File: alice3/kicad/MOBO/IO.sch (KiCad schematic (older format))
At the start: 12 parts, among them CON1 SD_Card, SW2 SOFT RESET, SW3 POWER, U6 MiniM4-D40, U7 DFROBOT_FTDI_BASIC

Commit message: Remove on/off switch.
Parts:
- removed SW3: POWER, Buttons_Switches_ThroughHole:SW_SPDT, symbol SPST
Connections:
- wire segments 76 -> 74
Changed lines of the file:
@@
 $EndDescr
 $Comp
-L +3.3V #PWR017
+L +3.3V #PWR019
 U 1 1 5689970E
 P 900 2900
-F 0 "#PWR017" H 900 2750 50  0001 C CNN
+F 0 "#PWR019" H 900 2750 50  0001 C CNN
 F 1 "+3.3V" H 900 3040 50  0000 C CNN
 F 2 "" H 900 2900 60  0000 C CNN
@@
 $EndComp
 $Comp
-L GND #PWR018
+L GND #PWR020
 U 1 1 5689975D
 P 2400 4600
-F 0 "#PWR018" H 2400 4350 50  0001 C CNN
+F 0 "#PWR020" H 2400 4350 50  0001 C CNN
 F 1 "GND" H 2400 4450 50  0000 C CNN
 F 2 "" H 2400 4600 60  0000 C CNN
@@
 NoConn ~ 7450 4700
 $Comp
-L GND #PWR019
+L GND #PWR021
 U 1 1 56899C9B
 P 8350 5900
-F 0 "#PWR019" H 8350 5650 50  0001 C CNN
+F 0 "#PWR021" H 8350 5650 50  0001 C CNN
 F 1 "GND" H 8350 5750 50  0000 C CNN
 F 2 "" H 8350 5900 60  0000 C CNN
@@
 $EndComp
 $Comp
-L +3.3V #PWR020
+L +3.3V #PWR022
 U 1 1 56899CD4
 P 8450 4050
-F 0 "#PWR020" H 8450 3900 50  0001 C CNN
+F 0 "#PWR022" H 8450 3900 50  0001 C CNN
 F 1 "+3.3V" H 8450 4190 50  0000 C CNN
 F 2 "" H 8450 4050 60  0000 C CNN
@@
 $EndComp
 $Comp
-L GND #PWR021
+L GND #PWR023
 U 1 1 568A1142
 P 900 4200
-F 0 "#PWR021" H 900 3950 50  0001 C CNN
+F 0 "#PWR023" H 900 3950 50  0001 C CNN
 F 1 "GND" H 900 4050 50  0000 C CNN
 F 2 "" H 900 4200 60  0000 C CNN
@@
 $EndComp
 $Comp
-L GND #PWR022
+L GND #PWR024
 U 1 1 568A2172
 P 5650 2550
-F 0 "#PWR022" H 5650 2300 50  0001 C CNN
+F 0 "#PWR024" H 5650 2300 50  0001 C CNN
 F 1 "GND" H 5650 2400 50  0000 C CNN
 F 2 "" H 5650 2550 60  0000 C CNN
@@
 $EndComp
 $Comp
-L GND #PWR023
+L GND #PWR025
 U 1 1 568A21B9
 P 6650 3150
-F 0 "#PWR023" H 6650 2900 50  0001 C CNN
+F 0 "#PWR025" H 6650 2900 50  0001 C CNN
 F 1 "GND" H 6650 3000 50  0000 C CNN
 F 2 "" H 6650 3150 60  0000 C CNN
@@
 $EndComp
 $Comp
-L +5V #PWR024
+L +5V #PWR026
 U 1 1 568DC45F
-P 8100 2700
-F 0 "#PWR024" H 8100 2550 50  0001 C CNN
-F 1 "+5V" H 8100 2840 50  0000 C CNN
-F 2 "" H 8100 2700 60  0000 C CNN
-F 3 "" H 8100 2700 60  0000 C CNN
-	1    8100 2700
+P 7000 2850
+F 0 "#PWR026" H 7000 2700 50  0001 C CNN
+F 1 "+5V" H 7000 2990 50  0000 C CNN
+F 2 "" H 7000 2850 60  0000 C CNN
+F 3 "" H 7000 2850 60  0000 C CNN
+	1    7000 2850
 	1    0    0    -1
 $EndComp
@@
 	5500 3150 5650 3150
 Wire Wire Line
-	8100 2850 8100 2700
-Wire Wire Line
 	2400 1600 2400 2000
 Wire Wire Line
@@
 Text GLabel 4000 2200 2    60   Input ~ 0
 /BUSACK
-$Comp
-L SPST SW3
-U 1 1 56A02251
-P 7500 2850
-F 0 "SW3" H 7500 2950 50  0000 C CNN
-F 1 "POWER" H 7500 2750 50  0000 C CNN
-F 2 "Buttons_Switches_ThroughHole:SW_SPDT" H 7500 2850 50  0001 C CNN
-F 3 "" H 7500 2850 50  0000 C CNN
-	1    7500 2850
-	1    0    0    -1
-$EndComp
-Wire Wire Line
-	8000 2850 8100 2850
 Wire Wire Line
 	7000 2850 6650 2850
@@
 	2450 4000 2700 4000
 $Comp
-L +3.3V #PWR025
+L +3.3V #PWR027
 U 1 1 56A03E02
 P 2400 1600
-F 0 "#PWR025" H 2400 1450 50  0001 C CNN
+F 0 "#PWR027" H 2400 1450 50  0001 C CNN
 F 1 "+3.3V" H 2400 1740 50  0000 C CNN
 F 2 "" H 2400 1600 60  0000 C CNN
@@
 $EndComp
 $Comp
-L GND #PWR026
+L GND #PWR028
 U 1 1 56A03E72
 P 1750 2200
-F 0 "#PWR026" H 1750 1950 50  0001 C CNN
+F 0 "#PWR028" H 1750 1950 50  0001 C CNN
 F 1 "GND" H 1750 2050 50  0000 C CNN
 F 2 "" H 1750 2200 60  0000 C CNN

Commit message: Before removing DFROBOT.
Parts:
- removed C3: 0.1µ, Capacitors_ThroughHole:C_Disc_D6_P5, symbol C
- renumbered C4 to C3
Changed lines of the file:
@@
 $EndDescr
 $Comp
-L +3.3V #PWR019
+L +3.3V #PWR19
 U 1 1 5689970E
 P 900 2900
-F 0 "#PWR019" H 900 2750 50  0001 C CNN
+F 0 "#PWR19" H 900 2750 50  0001 C CNN
 F 1 "+3.3V" H 900 3040 50  0000 C CNN
 F 2 "" H 900 2900 60  0000 C CNN
@@
 $EndComp
 $Comp
-L GND #PWR020
+L GND #PWR22
 U 1 1 5689975D
 P 2400 4600
-F 0 "#PWR020" H 2400 4350 50  0001 C CNN
+F 0 "#PWR22" H 2400 4350 50  0001 C CNN
 F 1 "GND" H 2400 4450 50  0000 C CNN
 F 2 "" H 2400 4600 60  0000 C CNN
@@
 NoConn ~ 7450 4700
 $Comp
-L GND #PWR021
+L GND #PWR26
 U 1 1 56899C9B
 P 8350 5900
-F 0 "#PWR021" H 8350 5650 50  0001 C CNN
+F 0 "#PWR26" H 8350 5650 50  0001 C CNN
 F 1 "GND" H 8350 5750 50  0000 C CNN
 F 2 "" H 8350 5900 60  0000 C CNN
@@
 $EndComp
 $Comp
-L +3.3V #PWR022
+L +3.3V #PWR27
 U 1 1 56899CD4
 P 8450 4050
-F 0 "#PWR022" H 8450 3900 50  0001 C CNN
+F 0 "#PWR27" H 8450 3900 50  0001 C CNN
 F 1 "+3.3V" H 8450 4190 50  0000 C CNN
 F 2 "" H 8450 4050 60  0000 C CNN
@@
 $EndComp
 $Comp
-L GND #PWR023
+L GND #PWR20
 U 1 1 568A1142
 P 900 4200
-F 0 "#PWR023" H 900 3950 50  0001 C CNN
+F 0 "#PWR20" H 900 3950 50  0001 C CNN
 F 1 "GND" H 900 4050 50  0000 C CNN
 F 2 "" H 900 4200 60  0000 C CNN
@@
 $EndComp
 $Comp
-L GND #PWR024
+L GND #PWR23
 U 1 1 568A2172
 P 5650 2550
-F 0 "#PWR024" H 5650 2300 50  0001 C CNN
+F 0 "#PWR23" H 5650 2300 50  0001 C CNN
 F 1 "GND" H 5650 2400 50  0000 C CNN
 F 2 "" H 5650 2550 60  0000 C CNN
@@
 $EndComp
 $Comp
-L GND #PWR025
+L GND #PWR24
 U 1 1 568A21B9
 P 6650 3150
-F 0 "#PWR025" H 6650 2900 50  0001 C CNN
+F 0 "#PWR24" H 6650 2900 50  0001 C CNN
 F 1 "GND" H 6650 3000 50  0000 C CNN
 F 2 "" H 6650 3150 60  0000 C CNN
@@
 NoConn ~ 5650 3050
 $Comp
-L CP1 C4
+L CP1 C3
 U 1 1 568A9C8C
 P 8150 5800
-F 0 "C4" H 8175 5900 50  0000 L CNN
+F 0 "C3" H 8175 5900 50  0000 L CNN
 F 1 "22µF" H 8175 5700 50  0000 L CNN
 F 2 "Capacitors_ThroughHole:C_Radial_D5_L11_P2.5" H 8150 5800 60  0001 C CNN
@@
 $EndComp
 $Comp
-L +5V #PWR026
+L +5V #PWR25
 U 1 1 568DC45F
 P 7000 2850
-F 0 "#PWR026" H 7000 2700 50  0001 C CNN
+F 0 "#PWR25" H 7000 2700 50  0001 C CNN
 F 1 "+5V" H 7000 2990 50  0000 C CNN
 F 2 "" H 7000 2850 60  0000 C CNN
@@
 	2450 4000 2700 4000
 $Comp
-L +3.3V #PWR027
+L +3.3V #PWR21
 U 1 1 56A03E02
 P 2400 1600
-F 0 "#PWR027" H 2400 1450 50  0001 C CNN
+F 0 "#PWR21" H 2400 1450 50  0001 C CNN
 F 1 "+3.3V" H 2400 1740 50  0000 C CNN
 F 2 "" H 2400 1600 60  0000 C CNN
@@
 	1    0    0    -1
 $EndComp
-$Comp
-L C C3
-U 1 1 56A03E30
-P 1750 1950
-F 0 "C3" H 1775 2050 50  0000 L CNN
-F 1 "0.1µ" H 1775 1850 50  0000 L CNN
-F 2 "Capacitors_ThroughHole:C_Disc_D6_P5" H 1788 1800 50  0001 C CNN
-F 3 "" H 1750 1950 50  0000 C CNN
-	1    1750 1950
-	1    0    0    -1
-$EndComp
-$Comp
-L GND #PWR028
-U 1 1 56A03E72
-P 1750 2200
-F 0 "#PWR028" H 1750 1950 50  0001 C CNN
-F 1 "GND" H 1750 2050 50  0000 C CNN
-F 2 "" H 1750 2200 60  0000 C CNN
-F 3 "" H 1750 2200 60  0000 C CNN
-	1    1750 2200
-	1    0    0    -1
-$EndComp
-Wire Wire Line
-	1750 2200 1750 2100
-Wire Wire Line
-	1750 1800 1750 1700
-Wire Wire Line
-	1750 1700 2400 1700
-Connection ~ 2400 1700
 Text GLabel 4300 3100 2    60   Input ~ 0
 /HALT

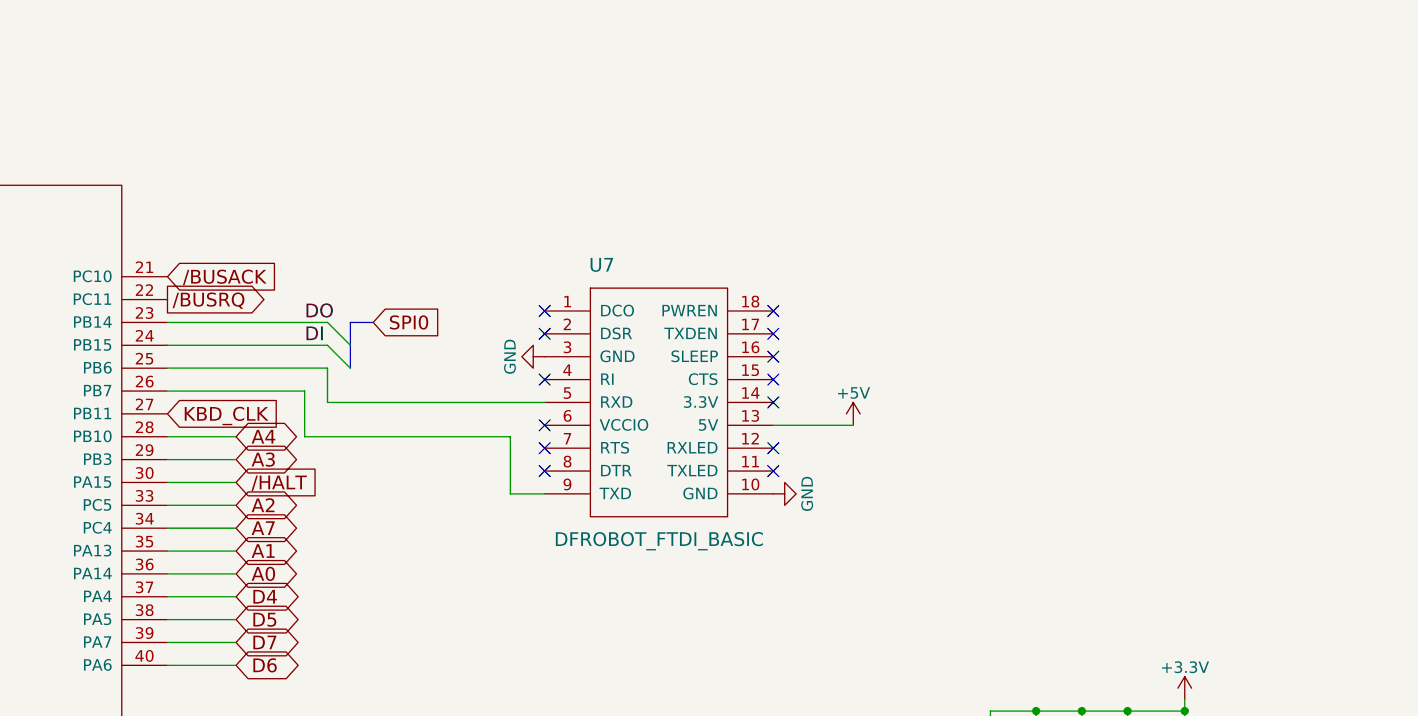
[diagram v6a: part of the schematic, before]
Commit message: Remove DFROBOT and LDO.
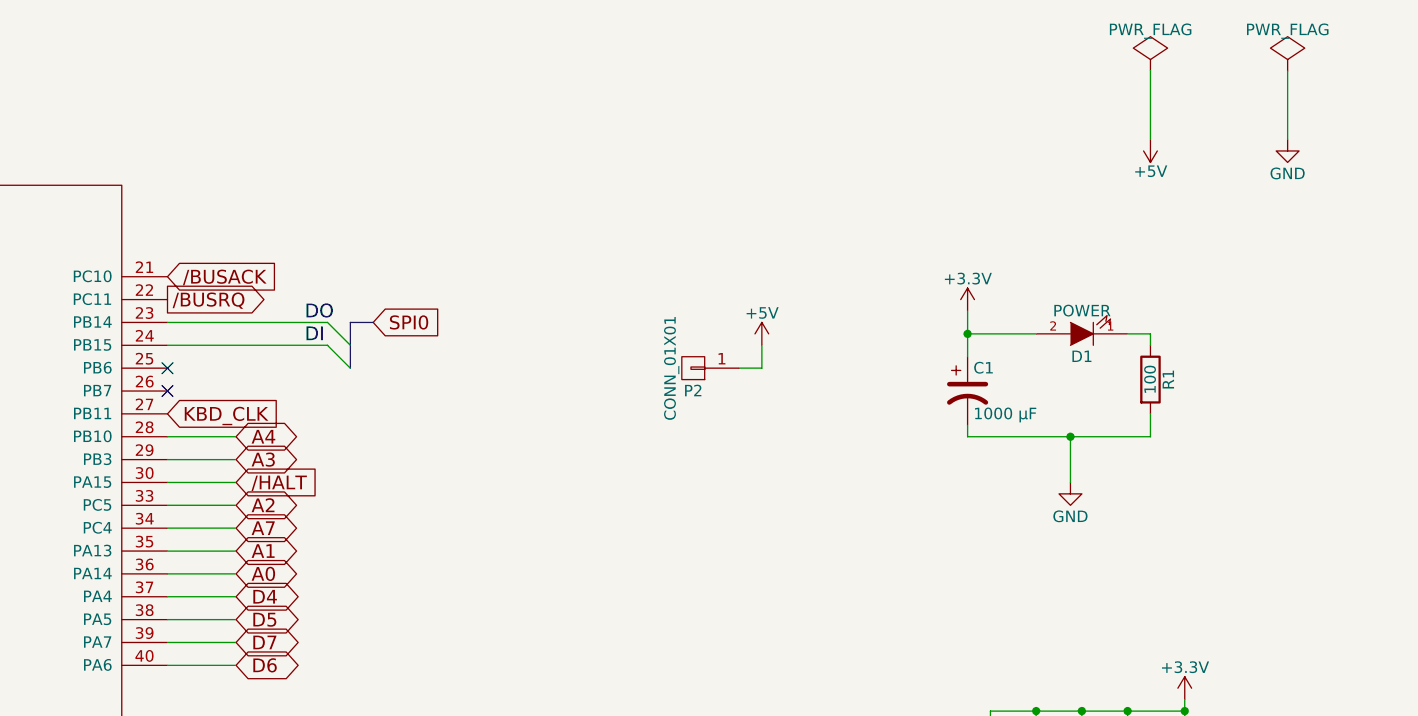
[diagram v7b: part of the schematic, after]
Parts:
- removed U7: DFROBOT_FTDI_BASIC, ftdi basic breakout:FTDIBASIC, symbol DFROBOT_FTDI_BASIC
- added C1: 1000 µF, Capacitors_ThroughHole:C_Radial_D8_L11.5_P3.5, symbol CP1
- added D1: POWER, LEDs:LED-5MM, symbol LED
- added P2: CONN_01X01, Pin_Headers:Pin_Header_Straight_1x01, symbol CONN_01X01
- added R1: 100, Resistors_ThroughHole:Resistor_Horizontal_RM10mm, symbol R
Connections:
- net +3V3: now also C1.1, D1.2 (A)
- net +5V: now also P2.1 (P1)
- net GND: now also C1.2, R1.2
- new net: D1.1 (K), R1.1
- no-connect marks 17 -> 6
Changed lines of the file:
@@
 $EndDescr
 $Comp
-L +3.3V #PWR19
+L +3.3V #PWR016
 U 1 1 5689970E
 P 900 2900
-F 0 "#PWR19" H 900 2750 50  0001 C CNN
+F 0 "#PWR016" H 900 2750 50  0001 C CNN
 F 1 "+3.3V" H 900 3040 50  0000 C CNN
 F 2 "" H 900 2900 60  0000 C CNN
@@
 $EndComp
 $Comp
-L GND #PWR22
+L GND #PWR017
 U 1 1 5689975D
 P 2400 4600
-F 0 "#PWR22" H 2400 4350 50  0001 C CNN
+F 0 "#PWR017" H 2400 4350 50  0001 C CNN
 F 1 "GND" H 2400 4450 50  0000 C CNN
 F 2 "" H 2400 4600 60  0000 C CNN
@@
 NoConn ~ 7450 4700
 $Comp
-L GND #PWR26
+L GND #PWR018
 U 1 1 56899C9B
 P 8350 5900
-F 0 "#PWR26" H 8350 5650 50  0001 C CNN
+F 0 "#PWR018" H 8350 5650 50  0001 C CNN
 F 1 "GND" H 8350 5750 50  0000 C CNN
 F 2 "" H 8350 5900 60  0000 C CNN
@@
 $EndComp
 $Comp
-L +3.3V #PWR27
+L +3.3V #PWR019
 U 1 1 56899CD4
 P 8450 4050
-F 0 "#PWR27" H 8450 3900 50  0001 C CNN
+F 0 "#PWR019" H 8450 3900 50  0001 C CNN
 F 1 "+3.3V" H 8450 4190 50  0000 C CNN
 F 2 "" H 8450 4050 60  0000 C CNN
@@
 $EndComp
 $Comp
-L GND #PWR20
+L GND #PWR020
 U 1 1 568A1142
 P 900 4200
-F 0 "#PWR20" H 900 3950 50  0001 C CNN
+F 0 "#PWR020" H 900 3950 50  0001 C CNN
 F 1 "GND" H 900 4050 50  0000 C CNN
 F 2 "" H 900 4200 60  0000 C CNN
@@
 	1    0    0    -1
 $EndComp
-$Comp
-L DFROBOT_FTDI_BASIC U7
-U 1 1 568A1F83
-P 6150 2750
-F 0 "U7" H 5900 3350 60  0000 C CNN
-F 1 "DFROBOT_FTDI_BASIC" H 6150 2150 60  0000 C CNN
-F 2 "ftdi basic breakout:FTDIBASIC" H 6150 2150 60  0001 C CNN
-F 3 "" H 6150 2150 60  0000 C CNN
-	1    6150 2750
-	1    0    0    -1
-$EndComp
-$Comp
-L GND #PWR23
-U 1 1 568A2172
-P 5650 2550
-F 0 "#PWR23" H 5650 2300 50  0001 C CNN
-F 1 "GND" H 5650 2400 50  0000 C CNN
-F 2 "" H 5650 2550 60  0000 C CNN
-F 3 "" H 5650 2550 60  0000 C CNN
-	1    5650 2550
-	0    1    1    0
-$EndComp
-$Comp
-L GND #PWR24
-U 1 1 568A21B9
-P 6650 3150
-F 0 "#PWR24" H 6650 2900 50  0001 C CNN
-F 1 "GND" H 6650 3000 50  0000 C CNN
-F 2 "" H 6650 3150 60  0000 C CNN
-F 3 "" H 6650 3150 60  0000 C CNN
-	1    6650 3150
-	0    -1   -1   0
-$EndComp
-NoConn ~ 6650 2350
-NoConn ~ 6650 2450
-NoConn ~ 6650 2550
-NoConn ~ 6650 2650
-NoConn ~ 6650 2750
-NoConn ~ 6650 2950
-NoConn ~ 6650 3050
-NoConn ~ 5650 2350
-NoConn ~ 5650 2450
-NoConn ~ 5650 2650
-NoConn ~ 5650 2850
-NoConn ~ 5650 2950
-NoConn ~ 5650 3050
 $Comp
 L CP1 C3
@@
 	1    8150 5800
 	0    -1   -1   0
-$EndComp
-$Comp
-L +5V #PWR25
-U 1 1 568DC45F
-P 7000 2850
-F 0 "#PWR25" H 7000 2700 50  0001 C CNN
-F 1 "+5V" H 7000 2990 50  0000 C CNN
-F 2 "" H 7000 2850 60  0000 C CNN
-F 3 "" H 7000 2850 60  0000 C CNN
-	1    7000 2850
-	1    0    0    -1
 $EndComp
 Text GLabel 2450 2900 0    60   Input ~ 0
@@
 	900  3700 2700 3700
 Wire Wire Line
-	5650 2750 4700 2750
-Wire Wire Line
-	4700 2750 4700 2600
-Wire Wire Line
-	4700 2600 4000 2600
-Wire Wire Line
-	4000 2700 4600 2700
-Wire Wire Line
-	4600 2700 4600 2900
-Wire Wire Line
-	4600 2900 5500 2900
-Wire Wire Line
-	5500 2900 5500 3150
-Wire Wire Line
-	5500 3150 5650 3150
-Wire Wire Line
 	2400 1600 2400 2000
 Wire Wire Line
@@
 Text GLabel 4000 2200 2    60   Input ~ 0
 /BUSACK
-Wire Wire Line
-	7000 2850 6650 2850
 Wire Wire Line
 	2450 2900 2700 2900
@@
 	2450 4000 2700 4000
 $Comp
-L +3.3V #PWR21
+L +3.3V #PWR021
 U 1 1 56A03E02
 P 2400 1600
-F 0 "#PWR21" H 2400 1450 50  0001 C CNN
+F 0 "#PWR021" H 2400 1450 50  0001 C CNN
 F 1 "+3.3V" H 2400 1740 50  0000 C CNN
 F 2 "" H 2400 1600 60  0000 C CNN
@@
 Wire Wire Line
 	4000 3100 4300 3100
+NoConn ~ 4000 2700
+NoConn ~ 4000 2600
+$Comp
+L CONN_01X01 P2
+U 1 1 56A07C53
+P 6300 2600
+F 0 "P2" H 6300 2700 50  0000 C CNN
+F 1 "CONN_01X01" V 6400 2600 50  0000 C CNN
+F 2 "Pin_Headers:Pin_Header_Straight_1x01" H 6300 2600 50  0001 C CNN
+F 3 "" H 6300 2600 50  0000 C CNN
+	1    6300 2600
+	-1   0    0    1
+$EndComp
+$Comp
+L +5V #PWR022
+U 1 1 56A07CCC
+P 6600 2500
+F 0 "#PWR022" H 6600 2350 50  0001 C CNN
+F 1 "+5V" H 6600 2640 50  0000 C CNN
+F 2 "" H 6600 2500 50  0000 C CNN
+F 3 "" H 6600 2500 50  0000 C CNN
+	1    6600 2500
+	1    0    0    -1
+$EndComp
+Wire Wire Line
+	6500 2600 6600 2600
+Wire Wire Line
+	6600 2600 6600 2500
+$Comp
+L PWR_FLAG #FLG023
+U 1 1 56A07E43
+P 8300 1300
+F 0 "#FLG023" H 8300 1395 50  0001 C CNN
+F 1 "PWR_FLAG" H 8300 1480 50  0000 C CNN
+F 2 "" H 8300 1300 50  0000 C CNN
+F 3 "" H 8300 1300 50  0000 C CNN
+	1    8300 1300
+	1    0    0    -1
+$EndComp
+$Comp
+L +5V #PWR024
+U 1 1 56A07E73
+P 8300 1600
+F 0 "#PWR024" H 8300 1450 50  0001 C CNN
+F 1 "+5V" H 8300 1740 50  0000 C CNN
+F 2 "" H 8300 1600 50  0000 C CNN
+F 3 "" H 8300 1600 50  0000 C CNN
+	1    8300 1600
+	-1   0    0    1
+$EndComp
+Wire Wire Line
+	8300 1300 8300 1600
+$Comp
+L PWR_FLAG #FLG025
+U 1 1 56A0800D
+P 8900 1300
+F 0 "#FLG025" H 8900 1395 50  0001 C CNN
+F 1 "PWR_FLAG" H 8900 1480 50  0000 C CNN
+F 2 "" H 8900 1300 50  0000 C CNN
+F 3 "" H 8900 1300 50  0000 C CNN
+	1    8900 1300
+	1    0    0    -1
+$EndComp
+$Comp
+L GND #PWR026
+U 1 1 56A08038
+P 8900 1600
+F 0 "#PWR026" H 8900 1350 50  0001 C CNN
+F 1 "GND" H 8900 1450 50  0000 C CNN
+F 2 "" H 8900 1600 50  0000 C CNN
+F 3 "" H 8900 1600 50  0000 C CNN
+	1    8900 1600
+	1    0    0    -1
+$EndComp
+Wire Wire Line
+	8900 1600 8900 1300
+$Comp
+L GND #PWR027
+U 1 1 56A0883B
+P 7950 3100
+F 0 "#PWR027" H 7950 2850 50  0001 C CNN
+F 1 "GND" H 7950 2950 50  0000 C CNN
+F 2 "" H 7950 3100 50  0000 C CNN
+F 3 "" H 7950 3100 50  0000 C CNN
+	1    7950 3100
+	1    0    0    -1
+$EndComp
+$Comp
+L +3.3V #PWR028
+U 1 1 56A08841
+P 7500 2350
+F 0 "#PWR028" H 7500 2200 50  0001 C CNN
+F 1 "+3.3V" H 7500 2490 50  0000 C CNN
+F 2 "" H 7500 2350 50  0000 C CNN
+F 3 "" H 7500 2350 50  0000 C CNN
+	1    7500 2350
+	1    0    0    -1
+$EndComp
+$Comp
+L CP1 C1
+U 1 1 56A08847
+P 7500 2700
+F 0 "C1" H 7525 2800 50  0000 L CNN
+F 1 "1000 µF" H 7525 2600 50  0000 L CNN
+F 2 "Capacitors_ThroughHole:C_Radial_D8_L11.5_P3.5" H 7500 2700 50  0001 C CNN
+F 3 "" H 7500 2700 50  0000 C CNN
+	1    7500 2700
+	1    0    0    -1
+$EndComp
+$Comp
+L LED D1
+U 1 1 56A0884E
+P 8000 2450
+F 0 "D1" H 8000 2550 50  0000 C CNN
+F 1 "POWER" H 8000 2350 50  0000 C CNN
+F 2 "LEDs:LED-5MM" H 8000 2450 50  0001 C CNN
+F 3 "" H 8000 2450 50  0000 C CNN
+	1    8000 2450
+	-1   0    0    1
+$EndComp
+$Comp
+L R R1
+U 1 1 56A08855
+P 8300 2650
+F 0 "R1" V 8380 2650 50  0000 C CNN
+F 1 "100" V 8300 2650 50  0000 C CNN
+F 2 "Resistors_ThroughHole:Resistor_Horizontal_RM10mm" V 8230 2650 50  0001 C CNN
+F 3 "" H 8300 2650 50  0000 C CNN
+	1    8300 2650
+	1    0    0    -1
+$EndComp
+Wire Wire Line
+	7500 2350 7500 2550
+Connection ~ 7500 2450
+Wire Wire Line
+	7500 2850 7500 2900
+Wire Wire Line
+	8200 2450 8300 2450
+Wire Wire Line
+	8300 2450 8300 2500
+Wire Wire Line
+	8300 2900 8300 2800
+Wire Wire Line
+	7950 3100 7950 2900
+Connection ~ 7950 2900
+Wire Wire Line
+	7800 2450 7500 2450
+Wire Wire Line
+	7500 2900 8300 2900
 $EndSCHEMATC

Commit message: Alice 3 v1 schematic and PCB, sent to OSHPark
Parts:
- C3: value 22µF -> 10µF
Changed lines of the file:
@@
 P 8150 5800
 F 0 "C3" H 8175 5900 50  0000 L CNN
-F 1 "22µF" H 8175 5700 50  0000 L CNN
+F 1 "10µF" H 8175 5700 50  0000 L CNN
 F 2 "Capacitors_ThroughHole:C_Radial_D5_L11_P2.5" H 8150 5800 60  0001 C CNN
 F 3 "" H 8150 5800 60  0000 C CNN
